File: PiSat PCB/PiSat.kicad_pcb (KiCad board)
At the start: 4 copper layers, 85 x 56 mm, 125 parts, among them IC1 PNT-SG3FS-TR, J1 Conn_01x05_Pin, J3 Conn_01x06_Pin, J4 Conn_01x03_Pin, J5 Conn_01x05_Pin, J6 Conn_01x05_Pin, Q7 AO3407A, SW1 MSK12C02, SW2 SKRPACE010, SW3 SKRPACE010, U1 BQ24075RGTR, U12 AP2112K-3.3, U4 DW03C_C41367942, U5 SMA-KWE_C7498154, U6 ESP32-C3-MINI-1U-N4, X1 X322512MSB4SI

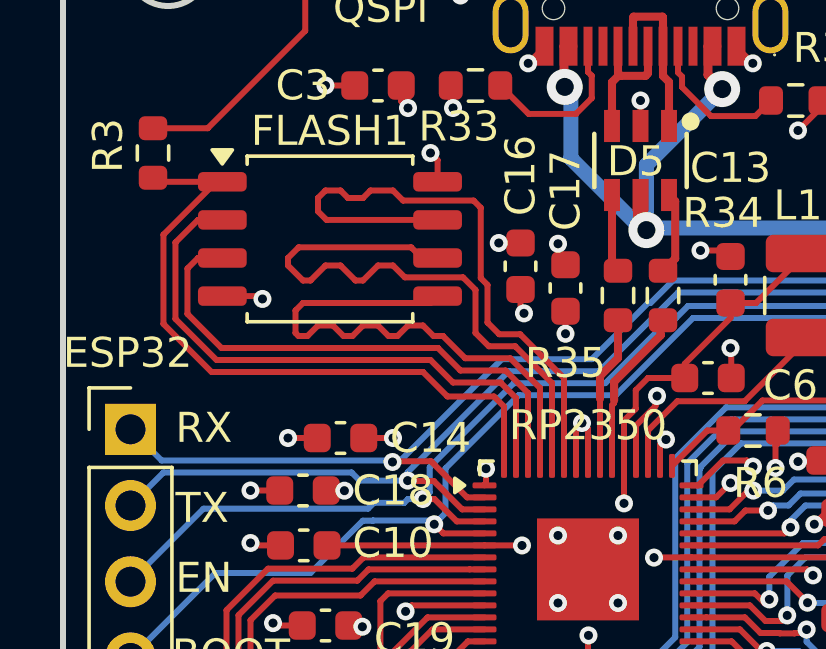
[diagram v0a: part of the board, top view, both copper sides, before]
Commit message: fixed flash ram wiring + added readme
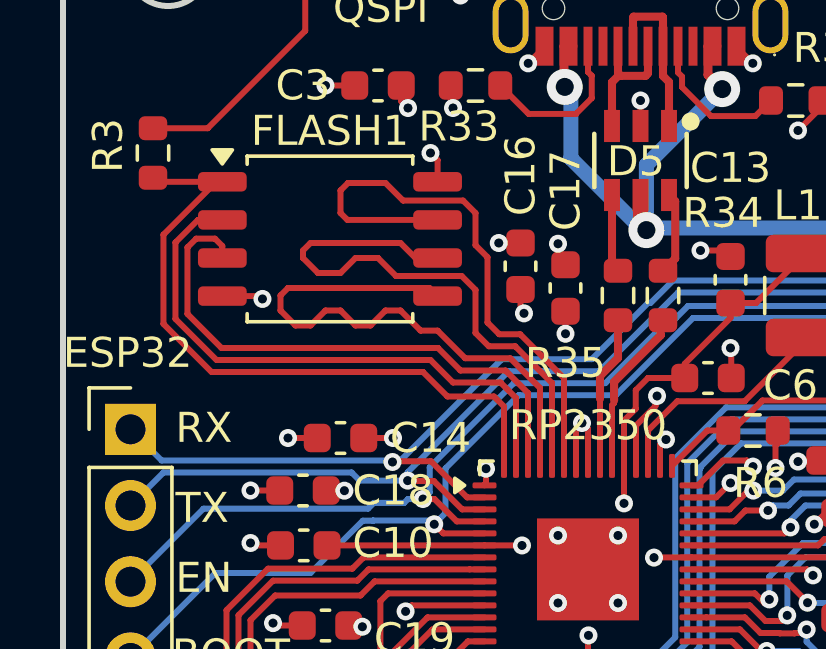
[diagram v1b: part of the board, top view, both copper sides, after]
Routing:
- net RP2350_QSPI_SD3: track 20.7 -> 19.4 mm
- net RP2350_QSPI_SD2: track 17.7 -> 18.9 mm
- net RP2350_QSPI_SCLK: track 20.4 -> 19.3 mm
- net RP2350_QSPI_SD0: track 18.1 -> 19.1 mm
